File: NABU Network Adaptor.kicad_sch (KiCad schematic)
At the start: 52 parts, among them J2 PC, J3 RF Module, J5 LEDs, U1 SN74LS164N, U10 UA9638CP, U11 UA9637ATC, U12 SN74LS164N, U13 SN74LS164N, U14 SN74LS04N, U15 SN74LS74AN, U16 N8X60N, U17 MN2114-4, U18 2114, U19 LM339N, U2 74LS30, U20 SN74LS164N, U21 SN74LS86N, U22 SN74LS74AN, U23 SN74LS74AN, U24 SN74LS04N, U26 SN74LS74AN, U27 SN74LS00P, U28 SN74LS74AN, U29 SN74LS74AN, U3 74LS27, U30 74LS02, U31 SC87253P, U32 SN74LS74AN, U33 MM74HCU04N, U4 SN74LS164N, U5 PAL16R6CN, U6 74LS374, U7 HD74LS373P, U8 110A332, U9 TRI863PL-02

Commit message: Fix up the flip-flops
U23 wasn't a flip-flop.
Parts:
- removed U23: SN74LS74AN, symbol 74xx:74LS74
- added R10, R12, R14, R17, R18, R33, R4, R5, R9: R, symbol Device:R
- added TP4, TP5: TestPoint, symbol Connector:TestPoint
- added U23: SN74LS00P, symbol 74xx:74LS00
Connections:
- net +5V: now also U28.12 (D), U32.2 (D), R10.2, R12.2, R14.1, R17.1, R33.1, R4.2, R5.2, R9.1
- net GND: now also U26.2 (D), R18.2; no longer U3.7 (GND)
- net at U22.10 (~{S}): now also U22.4 (~{S})
- net at U22.13 (~{R}): now also U22.2 (D)
- net at U15.12 (D): now also U15.8 (~{Q})
- net at U30.13: now also U28.11 (C)
- net at U33.6: now also U31.4 (Pin_4), U32.11 (C), U33.2, R18.1
- net at U27.1: now also U27.4
- net at U14.8, U27.5, U5.1 (Pin_1)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: now also U5.20 (Pin_20)
- net at TP2.1, U24.13, U3.12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: now also U22.3 (C)
- net at U7.1 (OE): now also U29.2 (D), U31.13 (Pin_13), R14.2, TP5.1
- net at U32.10 (~{S}): now also R17.2
- net at U32.12 (D): now also U9.17 (Pin_17), R33.2
- net at U32.13 (~{R}): now also R5.1
- net at U3.14 (VCC): now also U3.7 (GND)
- net at U22.1 (~{R}): now also R4.1
- net at U1.9 (~{MR}), U4.9 (~{MR}): no longer U22.4 (~{S})
- net at U22.6 (~{Q}): now also U26.11 (C)
- net at U29.10 (~{S}): now also U28.4 (~{S}), U29.4 (~{S}), U32.4 (~{S}), R12.1
- net at U29.12 (D): now also U29.5 (Q)
- net at U29.13 (~{R}): now also U29.1 (~{R})
- net at U29.8 (~{Q}): now also U28.3 (C)
- net at U28.1 (~{R}): now also U5.19 (Pin_19)
- net at U28.10 (~{S}): now also U27.11
- net at U28.13 (~{R}): now also U26.3 (C), U29.3 (C), U5.17 (Pin_17)
- net at U28.8 (~{Q}): now also U26.4 (~{S})
- net at U5.12 (Pin_12): now also U26.12 (D), U32.5 (Q)
- net at U32.1 (~{R}): now also U26.6 (~{Q}), U31.2 (Pin_2)
- net at U32.3 (C): now also U31.12 (Pin_12), TP4.1
- net at U26.1 (~{R}): now also U26.13 (~{R}), R10.1
- net at U26.10 (~{S}): now also R9.2
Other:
- moved on the sheet: TP1, TP2, TP3, U14B, U14C, U14D, U14G, U15A, U15B, U15C, U16, U17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

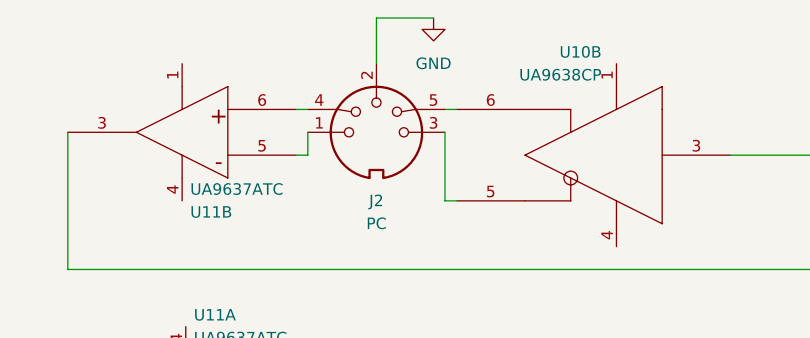
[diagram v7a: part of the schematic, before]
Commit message: RS-422 Pin 2 is NC, shell is grounded.
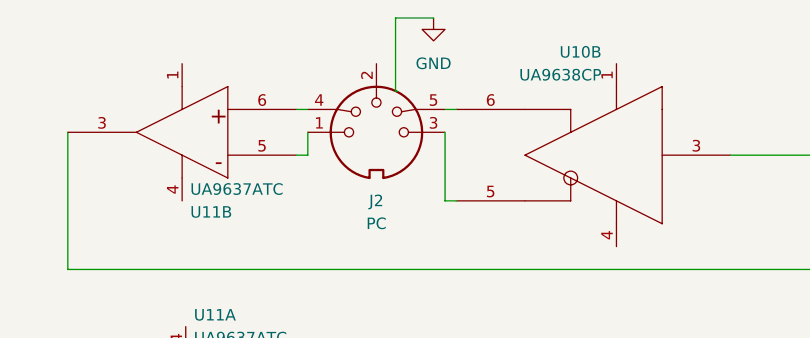
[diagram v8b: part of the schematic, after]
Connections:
- net GND: no longer J2.2
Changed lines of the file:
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@@
+    (stroke (width 0) (type default))
+  )
+  (wire (pts (xy 517.4896 147.8379) (xy 517.4896 147.813))
     (stroke (width 0) (type default))
   )
@@
     (stroke (width 0) (type default))
   )
+  (wire (pts (xy 517.3402 147.8379) (xy 517.4896 147.8379))
+    (stroke (width 0) (type default))
+  )
   (wire (pts (xy 173.99 579.12) (xy 739.14 579.12))
     (stroke (width 0) (type default))
@@
     (stroke (width 0) (type default))
   )
+  (wire (pts (xy 521.5653 139.7) (xy 517.3402 139.7))
+    (stroke (width 0) (type default))
+  )
   (wire (pts (xy 384.81 271.78) (xy 384.81 273.05))
     (stroke (width 0) (type default))
@@
     (stroke (width 0) (type default))
   )
+  (wire (pts (xy 517.3402 139.7) (xy 517.3402 147.8379))
+    (stroke (width 0) (type default))
+  )
   (wire (pts (xy 805.18 356.87) (xy 811.3796 356.87))
     (stroke (width 0) (type default))
@@
     (stroke (width 0) (type default))
   )
-  (wire (pts (xy 515.2153 139.7) (xy 521.5653 139.7))
-    (stroke (width 0) (type default))
-  )
   (wire (pts (xy 469.9 558.8) (xy 469.9 443.23))
     (stroke (width 0) (type default))
@@
     (stroke (width 0) (type default))
   )
-  (wire (pts (xy 515.2153 144.78) (xy 515.2153 139.7))
-    (stroke (width 0) (type default))
-  )
